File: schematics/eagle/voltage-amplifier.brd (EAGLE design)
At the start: 31.7 x 28.1 mm, 15 parts, among them Q1 2N3904, Q2 2N3904, Q3 2N3904, Q4 2N3904

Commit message: Cleanup
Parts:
- moved C5 0.76 mm to (14.9, 24.0)
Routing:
- net N$8: track 57.0 -> 55.1 mm
- net N$3: track 14.2 -> 12.5 mm
- net N$5: track 20.7 -> 19.4 mm
- net N$6: track 7.12 -> 6.36 mm
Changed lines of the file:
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@@
 <param name="PrefDir.14" value="0"/>
 <param name="PrefDir.15" value="0"/>
-<param name="PrefDir.16" value="0"/>
+<param name="PrefDir.16" value="-"/>
 <param name="cfVia" value="8"/>
 <param name="cfNonPref" value="5"/>
@@
 <elements>
 <element name="C4" library="sym" package="C0805" value="10u" x="7.112" y="7.366" smashed="yes" rot="R180">
-<attribute name="NAME" x="7.366" y="5.969" size="1.27" layer="25" rot="R180"/>
+<attribute name="NAME" x="11.43" y="8.128" size="1.27" layer="25" rot="R180"/>
 <attribute name="VALUE" x="8.382" y="9.906" size="1.27" layer="27" rot="R180"/>
 </element>
-<element name="C5" library="sym" package="C0805" value="10u" x="14.097" y="24.003" smashed="yes" rot="R180">
-<attribute name="NAME" x="15.24" y="26.289" size="1.27" layer="25" rot="R180"/>
-<attribute name="VALUE" x="15.367" y="26.543" size="1.27" layer="27" rot="R180"/>
+<element name="C5" library="sym" package="C0805" value="10u" x="14.859" y="24.003" smashed="yes" rot="R180">
+<attribute name="NAME" x="16.002" y="26.289" size="1.27" layer="25" rot="R180"/>
+<attribute name="VALUE" x="16.129" y="26.543" size="1.27" layer="27" rot="R180"/>
 </element>
 <element name="C6" library="sym" package="C0805" value="10u" x="14.097" y="7.493" smashed="yes" rot="R180">
@@
 </element>
 <element name="Q2" library="sym" package="SOT23" value="2N3904" x="7.112" y="19.05" smashed="yes">
-<attribute name="NAME" x="3.048" y="18.669" size="1.27" layer="25"/>
+<attribute name="NAME" x="8.636" y="18.542" size="1.27" layer="25"/>
 <attribute name="VALUE" x="5.207" y="15.875" size="1.27" layer="27"/>
 </element>
@@
 <contactref element="R4" pad="1"/>
 <contactref element="R3" pad="1"/>
-<wire x1="25.997" y1="7.94" x2="22.1000625" y2="7.94" width="0.7" layer="1"/>
-<wire x1="22.1000625" y1="7.94" x2="22.032" y2="7.874" width="0.7" layer="1"/>
-<wire x1="25.997" y1="7.94" x2="26.101" y2="7.62" width="0.7" layer="1"/>
+<wire x1="26.101" y1="7.62" x2="25.847" y2="7.874" width="0.7" layer="1"/>
+<wire x1="25.847" y1="7.874" x2="22.032" y2="7.874" width="0.7" layer="1"/>
 </signal>
 <signal name="N$3">
@@
 <contactref element="Q1" pad="3"/>
 <contactref element="R5" pad="2"/>
-<wire x1="25.121" y1="21.74" x2="27.74" y2="21.74" width="0.7" layer="1"/>
-<wire x1="22.121" y1="18.74" x2="25.121" y2="21.74" width="0.7" layer="1"/>
-<wire x1="22.121" y1="17.54" x2="22.121" y2="18.74" width="0.7" layer="1"/>
-<wire x1="27.74" y1="21.74" x2="28.067" y2="21.887" width="0.7" layer="1"/>
-<wire x1="22.121" y1="17.54" x2="22.545" y2="17.399" width="0.7" layer="1"/>
-<wire x1="22.121" y1="16.94" x2="22.121" y2="12.74" width="0.7" layer="1"/>
-<wire x1="22.121" y1="12.74" x2="22.545" y2="12.446" width="0.7" layer="1"/>
-<wire x1="22.121" y1="16.94" x2="22.545" y2="17.399" width="0.7" layer="1"/>
+<wire x1="27.92" y1="21.74" x2="28.067" y2="21.887" width="0.7" layer="1"/>
+<wire x1="22.545" y1="17.399" x2="22.545" y2="17.6095" width="0.7" layer="1"/>
+<wire x1="22.545" y1="17.6095" x2="26.6755" y2="21.74" width="0.7" layer="1"/>
+<wire x1="26.6755" y1="21.74" x2="27.92" y2="21.74" width="0.7" layer="1"/>
+<wire x1="22.545" y1="17.399" x2="22.545" y2="12.446" width="0.7" layer="1"/>
 </signal>
 <signal name="VOUT">
@@
 <contactref element="C5" pad="2"/>
 <contactref element="Q3" pad="3"/>
-<wire x1="13.94" y1="21.74" x2="13.94" y2="20.54" width="0.7" layer="1"/>
-<wire x1="12.74" y1="22.94" x2="13.94" y2="21.74" width="0.7" layer="1"/>
-<wire x1="12.74" y1="23.54" x2="12.74" y2="22.94" width="0.7" layer="1"/>
-<wire x1="13.94" y1="20.54" x2="14.097" y2="20.023" width="0.7" layer="1"/>
-<wire x1="12.74" y1="23.54" x2="13.147" y2="24.003" width="0.7" layer="1"/>
-<wire x1="20.132" y1="7.874" x2="19.629" y2="7.874" width="0.7" layer="1"/>
-<wire x1="14.097" y1="20.023" x2="14.18" y2="19.94" width="0.7" layer="1"/>
-<wire x1="14.18" y1="19.94" x2="16.0391875" y2="19.94" width="0.7" layer="1"/>
-<wire x1="16.0391875" y1="19.94" x2="19.629" y2="16.3501875" width="0.7" layer="1"/>
-<wire x1="19.629" y1="16.3501875" x2="19.629" y2="7.874" width="0.7" layer="1"/>
+<wire x1="13.97" y1="20.15" x2="14.097" y2="20.023" width="0.7" layer="1"/>
+<wire x1="19.629" y1="8.377" x2="20.132" y2="7.874" width="0.7" layer="1"/>
+<wire x1="13.909" y1="24.003" x2="13.97" y2="23.942" width="0.7" layer="1"/>
+<wire x1="13.97" y1="23.942" x2="13.97" y2="20.15" width="0.7" layer="1"/>
+<wire x1="14.097" y1="20.023" x2="15.25116875" y2="20.023" width="0.7" layer="1"/>
+<wire x1="15.25116875" y1="20.023" x2="19.629" y2="15.64516875" width="0.7" layer="1"/>
+<wire x1="19.629" y1="15.64516875" x2="19.629" y2="8.377" width="0.7" layer="1"/>
 </signal>
 <signal name="N$6">
 <contactref element="R2" pad="2"/>
 <contactref element="C5" pad="1"/>
-<wire x1="15.047" y1="24.003" x2="22.164" y2="24.003" width="0.7" layer="1"/>
+<wire x1="15.809" y1="24.003" x2="22.164" y2="24.003" width="0.7" layer="1"/>
 </signal>
 <signal name="N$7">
@@
 <contactref element="Q3" pad="2"/>
 <contactref element="Q2" pad="3"/>
-<wire x1="7.34" y1="20.54" x2="8.54" y2="20.54" width="0.7" layer="1"/>
-<wire x1="7.34" y1="20.54" x2="7.112" y2="20.15" width="0.7" layer="1"/>
-<wire x1="8.54" y1="20.54" x2="8.54" y2="23.54" width="0.7" layer="1"/>
-<wire x1="8.54" y1="23.54" x2="8.062" y2="24.13" width="0.7" layer="1"/>
-<wire x1="15" y1="16.2" x2="15" y2="17.4" width="0.7" layer="1"/>
-<wire x1="17.4" y1="13.8" x2="15" y2="16.2" width="0.7" layer="1"/>
-<wire x1="17.4" y1="6" x2="17.4" y2="13.8" width="0.7" layer="1"/>
-<wire x1="13.73" y1="2.33" x2="17.4" y2="6" width="0.7" layer="1"/>
-<wire x1="1.765" y1="2.33" x2="13.73" y2="2.33" width="0.7" layer="1"/>
-<wire x1="1.765" y1="16.765" x2="1.765" y2="2.33" width="0.7" layer="1"/>
-<wire x1="5.4" y1="20.4" x2="1.765" y2="16.765" width="0.7" layer="1"/>
-<wire x1="7.2" y1="20.4" x2="5.4" y2="20.4" width="0.7" layer="1"/>
-<wire x1="15" y1="17.4" x2="15.047" y2="17.823" width="0.7" layer="1"/>
-<wire x1="7.2" y1="20.4" x2="7.112" y2="20.15" width="0.7" layer="1"/>
+<wire x1="8.062" y1="24.13" x2="8.032" y2="24.1" width="0.7" layer="1"/>
+<wire x1="8.032" y1="24.1" x2="8.032" y2="21.07" width="0.7" layer="1"/>
+<wire x1="8.032" y1="21.07" x2="7.112" y2="20.15" width="0.7" layer="1"/>
+<wire x1="7.112" y1="20.15" x2="2.6415" y2="20.15" width="0.7" layer="1"/>
+<wire x1="2.6415" y1="20.15" x2="1.9" y2="19.4085" width="0.7" layer="1"/>
+<wire x1="1.9" y1="19.4085" x2="1.9" y2="3.1" width="0.7" layer="1"/>
+<wire x1="1.9" y1="3.1" x2="13.48533125" y2="3.1" width="0.7" layer="1"/>
+<wire x1="13.48533125" y1="3.1" x2="17.4" y2="7.01466875" width="0.7" layer="1"/>
+<wire x1="17.4" y1="7.01466875" x2="17.4" y2="15.324" width="0.7" layer="1"/>
+<wire x1="17.4" y1="15.324" x2="15.047" y2="17.677" width="0.7" layer="1"/>
+<wire x1="15.047" y1="17.677" x2="15.047" y2="17.823" width="0.7" layer="1"/>
 </signal>
 <signal name="VIN">
@@
 <wire x1="15.6" y1="7.8" x2="15.047" y2="7.493" width="0.7" layer="1"/>
 <wire x1="15.6" y1="12" x2="15.047" y2="12.573" width="0.7" layer="1"/>
-<wire x1="29.4" y1="19.8" x2="29.4" y2="12.6" width="0.7" layer="1"/>
-<wire x1="30" y1="20.4" x2="29.4" y2="19.8" width="0.7" layer="1"/>
-<wire x1="30" y1="23.4" x2="30" y2="20.4" width="0.7" layer="1"/>
-<wire x1="29.4" y1="24" x2="30" y2="23.4" width="0.7" layer="1"/>
-<wire x1="29.4" y1="12.6" x2="29.144" y2="12.403" width="0.7" layer="1"/>
-<wire x1="29.4" y1="24" x2="29.017" y2="24.087" width="0.7" layer="1"/>
+<wire x1="29.017" y1="24.087" x2="29.767" y2="23.337" width="0.7" layer="1"/>
+<wire x1="29.767" y1="23.337" x2="29.767" y2="13.026" width="0.7" layer="1"/>
+<wire x1="29.767" y1="13.026" x2="29.144" y2="12.403" width="0.7" layer="1"/>
 <wire x1="15.047" y1="12.573" x2="29.144" y2="12.403" width="0" layer="19" extent="1-1"/>
 <wire x1="6.162" y1="17.95" x2="15.047" y2="12.573" width="0" layer="19" extent="1-1"/>
@@
 <wire x1="12.6" y1="7.2" x2="10.2" y2="4.8" width="0.7" layer="1"/>
 <wire x1="6" y1="12.6" x2="6.162" y2="12.7" width="0.7" layer="1"/>
-<wire x1="12.6" y1="7.2" x2="13.147" y2="7.493" width="0.7" layer="1"/>
+<wire x1="13.147" y1="7.493" x2="12.6" y2="7.2" width="0.7" layer="1"/>
 </signal>
 <signal name="N$4">

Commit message: Voltage Amplifier PCB
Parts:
- C4, C5, C6: device sym:C0805 -> sym-toh:C050-025X075
- Q1, Q2, Q3, Q4: device sym:SOT23 -> sym-toh:TO92
- R1, R2, R3, R4, R5, R6, R7, R8: device sym:R0805 -> sym-toh:0207/7
- moved Q1 19.1 mm to (28.7, 3.94), turned to 0 degrees
- moved R4 18.4 mm to (38.9, 21.7)
- moved R5 15.4 mm to (38.9, 11.6), turned to 0 degrees
- moved R1 15.4 mm to (38.9, 16.6)
- moved R3 15.2 mm to (27.4, 21.7)
- moved C5 14.6 mm to (27.4, 16.6)
- moved R2 13.2 mm to (27.4, 11.6)
- moved Q4 11.9 mm to (37.6, 3.94), turned to 0 degrees
- moved R6 8.29 mm to (15.1, 22.0), turned to 180 degrees
- moved R7 6.19 mm to (8.76, 6.73), turned to 90 degrees
- moved R8 5.85 mm to (13.8, 6.73), turned to 270 degrees
- moved Q3 5.11 mm to (16.4, 14.4)
- moved C6 4.89 mm to (18.9, 6.73), turned to 90 degrees
- moved Q2 4.05 mm to (4.95, 15.6)
- moved C4 3.49 mm to (3.68, 6.73), turned to 270 degrees
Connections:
- removed net N$4: R1.1
- removed net N$9: R6.1
- net V+: now also R1.1, R6.1
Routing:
- net 0: track 17.9 -> 60.8 mm
- net VOUT: track 4.19 -> 37.3 mm
- net N$8: track 55.1 -> 30.1 mm, vias 0 -> 2
- net V+: track 4.17 -> 27.5 mm
- net N$3: track 12.5 -> 29.2 mm
- net N$11: track 29.7 -> 21.1 mm
- net N$10: track 11.6 -> 15.9 mm
- net N$1: track 2.82 -> 6.79 mm
- net N$7: track 3.09 -> 6.77 mm
- net N$6: track 6.36 -> 9.18 mm
- net N$5: track 19.4 -> 18.7 mm
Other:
- board size 31.7 x 28.1 mm -> 45.8 x 24.6 mm

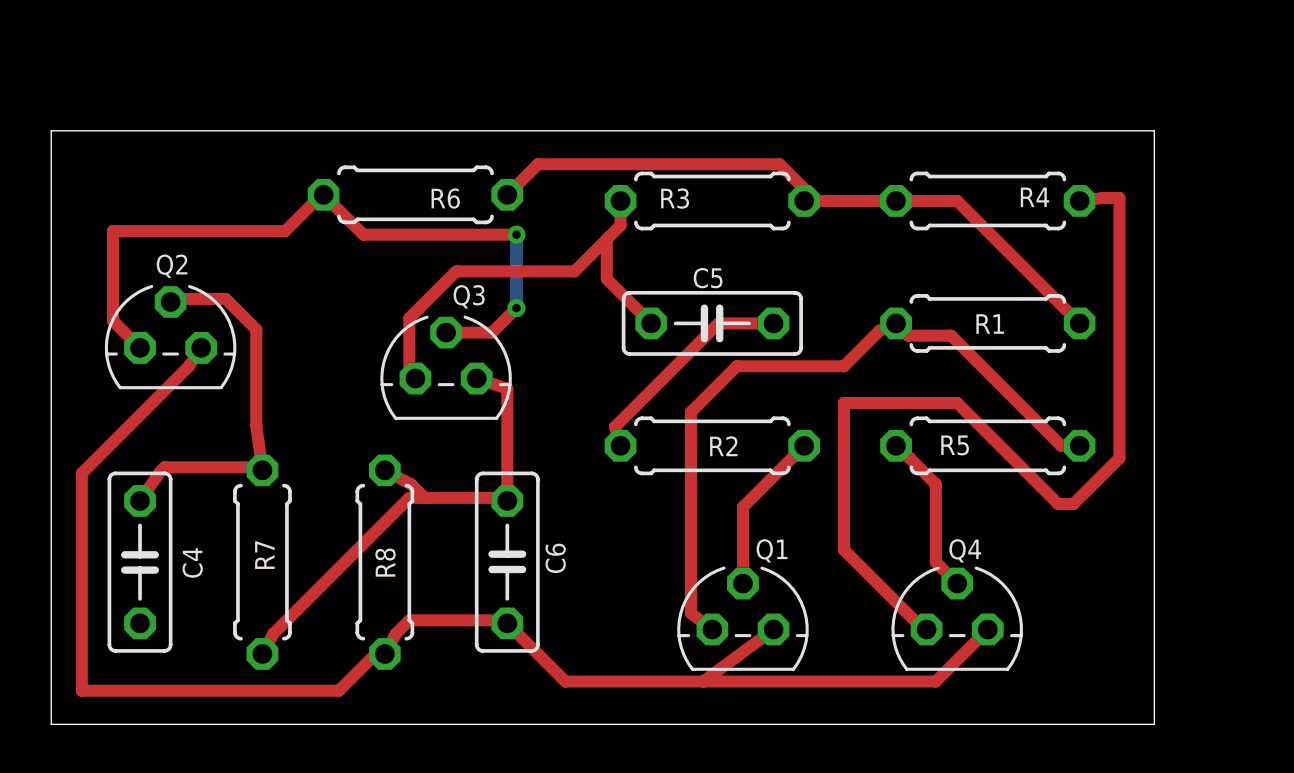
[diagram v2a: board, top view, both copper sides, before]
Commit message: Increased Voltage Amplifier Spacing
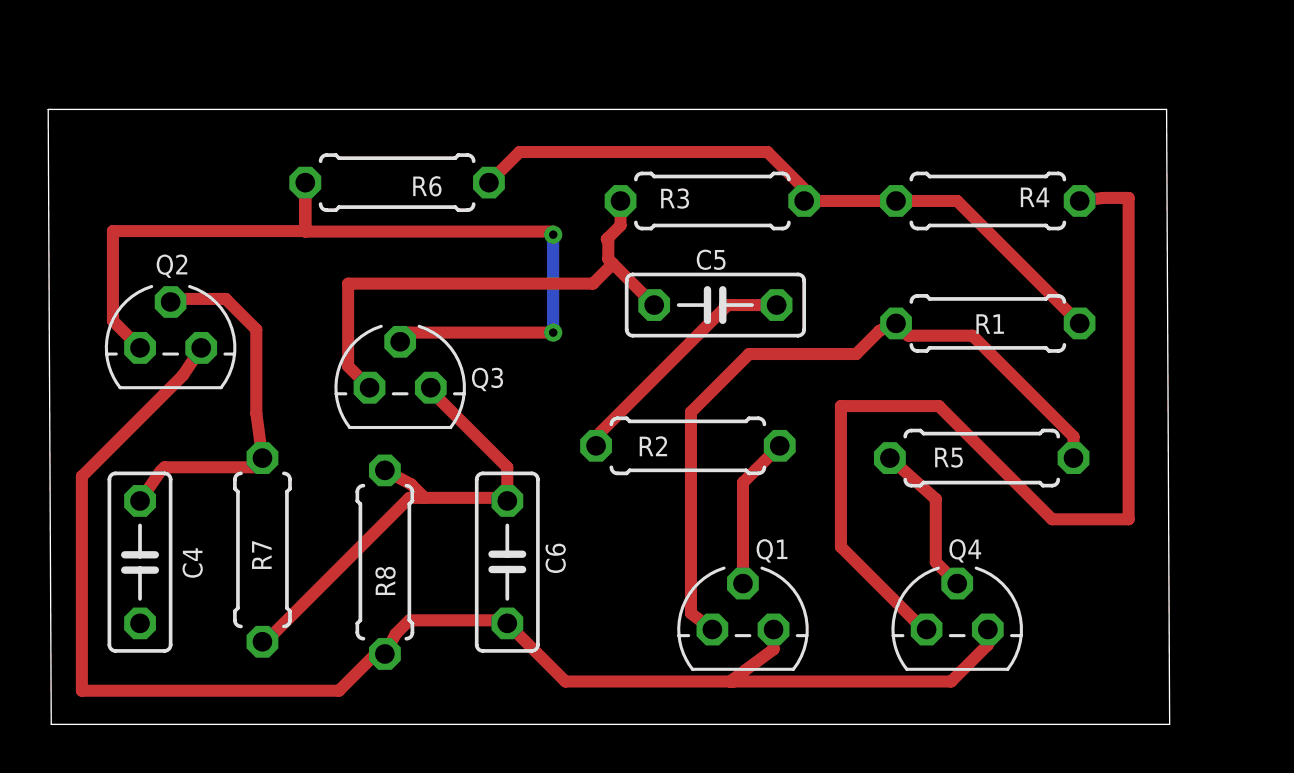
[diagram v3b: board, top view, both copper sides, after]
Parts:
- moved Q3 1.94 mm to (14.5, 14.0)
- moved R2 1.02 mm to (26.4, 11.6)
- moved R6 0.92 mm to (14.4, 22.5)
- moved C5 0.77 mm to (27.6, 17.4)
- moved R5 0.57 mm to (38.6, 11.0)
- moved R7 0.51 mm to (8.76, 7.24)
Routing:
- net N$8: track 30.1 -> 38.6 mm
- net N$5: track 18.7 -> 21.9 mm
- net VOUT: track 37.3 -> 40.0 mm
- net N$6: track 9.18 -> 10.2 mm
- net V+: track 27.5 -> 28.5 mm
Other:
- board size 45.8 x 24.6 mm -> 46.5 x 25.5 mm
